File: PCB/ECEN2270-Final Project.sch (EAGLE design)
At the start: 39 parts, among them J1 USB_MINI-B_SMT, J2 POWER_JACK, Q1 310mA/60V/1.6Ω, Q2 2.5A/30V/105mΩ, U1 FT231XS, U2 LMV358, U3 ATMEGA328P_TQFP, U4 3.3V/150mA, Y2 16MHz

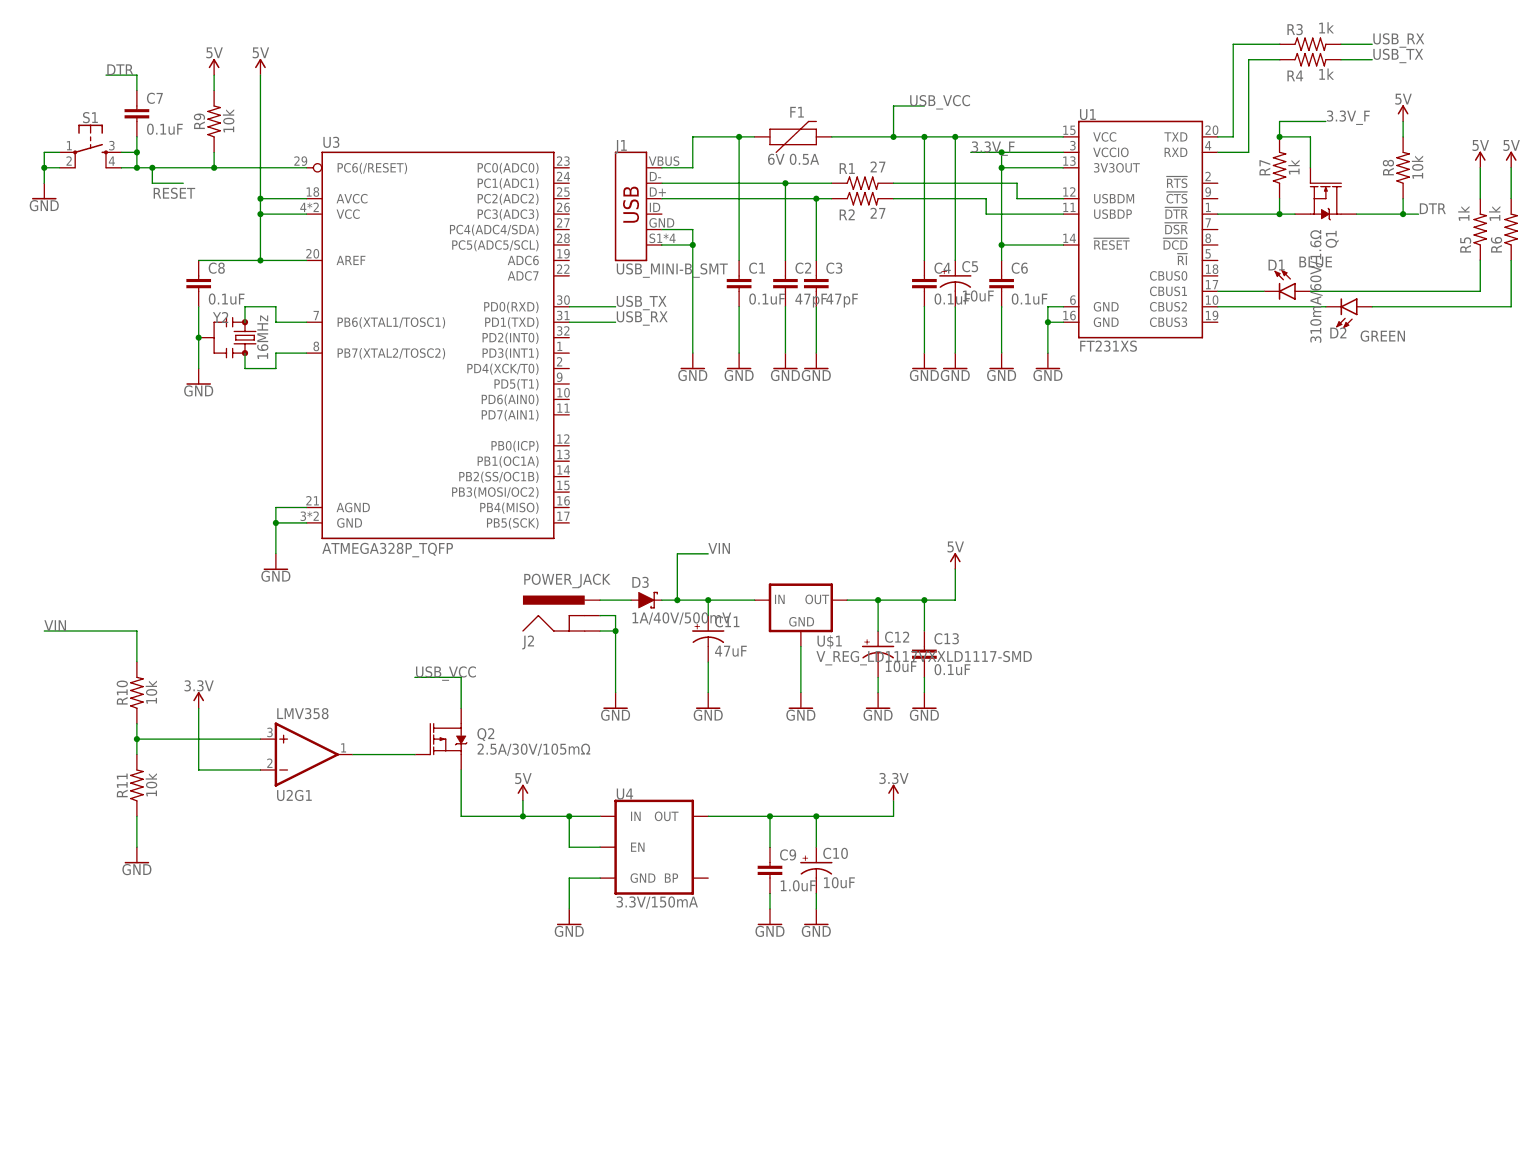
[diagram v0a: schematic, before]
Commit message: Added ICSP Header For Arduino
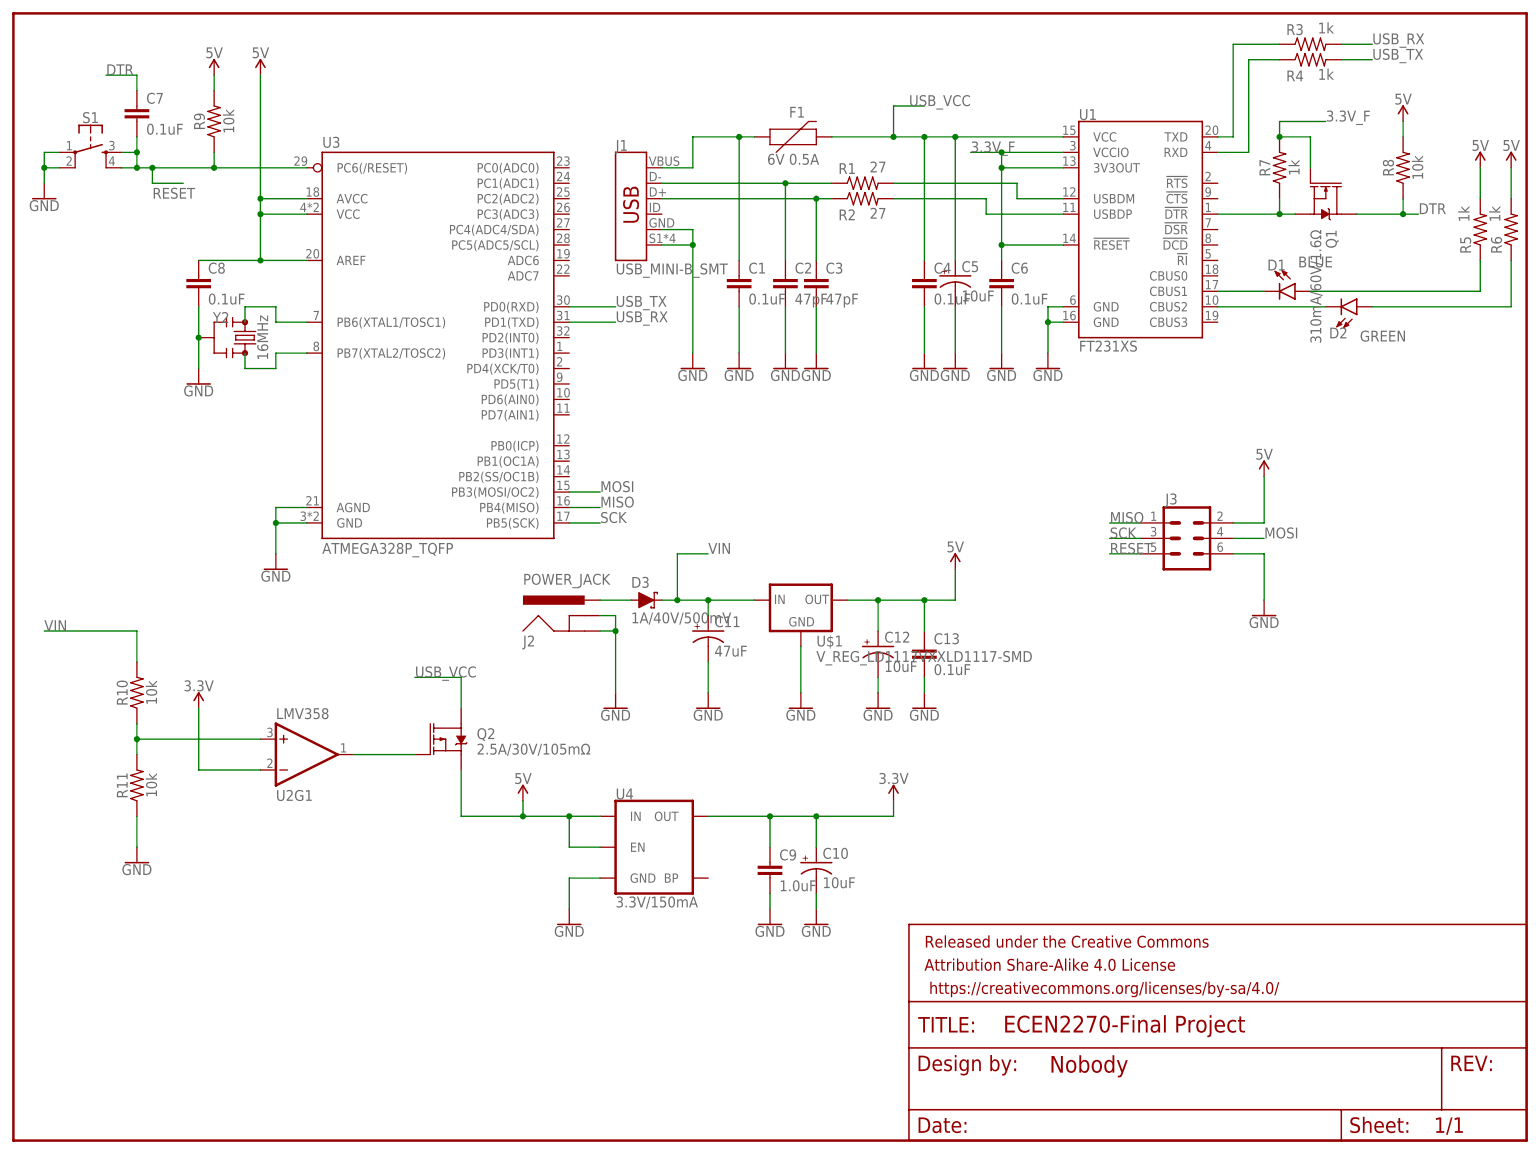
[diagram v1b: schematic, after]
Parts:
- added FRAME1: FRAME-LETTERNO_PACKAGE, SparkFun-Aesthetics:FRAME-LETTERNO_PACKAGE
- added J3: (no value), SparkFun-Connectors:CONN_03X22X3_SILK_MALE_PTH
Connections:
- new net MISO: J3.1, U3.PB4(MISO)
- new net MOSI: J3.4, U3.PB3(MOSI/OC2)
- new net SCK: J3.3, U3.PB5(SCK)
- net 5V: now also J3.2
- net GND: now also J3.6
- net RESET: now also J3.5
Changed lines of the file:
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@@
 <part name="C13" library="SparkFun-Capacitors" deviceset="0.1UF" device="-0603-25V-(+80/-20%)" value="0.1uF"/>
 <part name="SUPPLY9" library="SparkFun-PowerSymbols" deviceset="5V" device=""/>
+<part name="FRAME1" library="SparkFun-Aesthetics" deviceset="FRAME-LETTER" device="NO_PACKAGE"/>
+<part name="J3" library="SparkFun-Connectors" deviceset="CONN_03X2" device="2X3_SILK_MALE_PTH"/>
+<part name="SUPPLY10" library="SparkFun-PowerSymbols" deviceset="5V" device=""/>
+<part name="GND21" library="SparkFun-PowerSymbols" deviceset="GND" device=""/>
 </parts>
 <sheets>
@@
 <instance part="SUPPLY9" gate="G$1" x="154.94" y="93.98" smashed="yes">
 <attribute name="VALUE" x="154.94" y="96.774" size="1.778" layer="96" align="bottom-center"/>
+</instance>
+<instance part="FRAME1" gate="G$1" x="0" y="0" smashed="yes"/>
+<instance part="FRAME1" gate="V" x="147.32" y="0" smashed="yes">
+<attribute name="LAST_DATE_TIME" x="160.02" y="1.27" size="2.54" layer="94" font="vector"/>
+<attribute name="SHEET" x="233.68" y="1.27" size="2.54" layer="94" font="vector"/>
+<attribute name="DRAWING_NAME" x="162.814" y="17.78" size="2.7432" layer="94" font="vector"/>
+<attribute name="DESIGNER" x="170.434" y="11.176" size="2.7432" layer="94" font="vector"/>
+</instance>
+<instance part="J3" gate="G$1" x="193.04" y="99.06" smashed="yes">
+<attribute name="NAME" x="189.484" y="104.648" size="1.778" layer="95" font="vector"/>
+<attribute name="VALUE" x="189.738" y="93.218" size="1.778" layer="96" font="vector" align="top-left"/>
+</instance>
+<instance part="SUPPLY10" gate="G$1" x="205.74" y="109.22" smashed="yes">
+<attribute name="VALUE" x="205.74" y="112.014" size="1.778" layer="96" align="bottom-center"/>
+</instance>
+<instance part="GND21" gate="1" x="205.74" y="86.36" smashed="yes">
+<attribute name="VALUE" x="205.74" y="86.106" size="1.778" layer="96" align="top-center"/>
 </instance>
 </instances>
@@
 <wire x1="149.86" y1="73.66" x2="149.86" y2="76.2" width="0.1524" layer="91"/>
 </segment>
+<segment>
+<pinref part="J3" gate="G$1" pin="6"/>
+<wire x1="200.66" y1="96.52" x2="205.74" y2="96.52" width="0.1524" layer="91"/>
+<wire x1="205.74" y1="96.52" x2="205.74" y2="88.9" width="0.1524" layer="91"/>
+<pinref part="GND21" gate="1" pin="GND"/>
+</segment>
 </net>
 <net name="3.3V_F" class="0">
@@
 <wire x1="154.94" y1="88.9" x2="154.94" y2="93.98" width="0.1524" layer="91"/>
 <pinref part="SUPPLY9" gate="G$1" pin="5V"/>
+</segment>
+<segment>
+<pinref part="J3" gate="G$1" pin="2"/>
+<wire x1="200.66" y1="101.6" x2="205.74" y2="101.6" width="0.1524" layer="91"/>
+<wire x1="205.74" y1="101.6" x2="205.74" y2="109.22" width="0.1524" layer="91"/>
+<pinref part="SUPPLY10" gate="G$1" pin="5V"/>
 </segment>
 </net>
@@
 <label x="22.86" y="154.94" size="1.778" layer="95"/>
 </segment>
+<segment>
+<pinref part="J3" gate="G$1" pin="5"/>
+<wire x1="185.42" y1="96.52" x2="180.34" y2="96.52" width="0.1524" layer="91"/>
+<label x="180.34" y="96.52" size="1.778" layer="95"/>
+</segment>
 </net>
 <net name="N$13" class="0">
@@
 </segment>
 </net>
+<net name="MISO" class="0">
+<segment>
+<pinref part="J3" gate="G$1" pin="1"/>
+<wire x1="185.42" y1="101.6" x2="180.34" y2="101.6" width="0.1524" layer="91"/>
+<label x="180.34" y="101.6" size="1.778" layer="95"/>
+</segment>
+<segment>
+<pinref part="U3" gate="U1" pin="PB4(MISO)"/>
+<wire x1="91.44" y1="104.14" x2="96.52" y2="104.14" width="0.1524" layer="91"/>
+<label x="96.52" y="104.14" size="1.778" layer="95"/>
+</segment>
+</net>
+<net name="SCK" class="0">
+<segment>
+<pinref part="J3" gate="G$1" pin="3"/>
+<wire x1="185.42" y1="99.06" x2="180.34" y2="99.06" width="0.1524" layer="91"/>
+<label x="180.34" y="99.06" size="1.778" layer="95"/>
+</segment>
+<segment>
+<pinref part="U3" gate="U1" pin="PB5(SCK)"/>
+<wire x1="91.44" y1="101.6" x2="96.52" y2="101.6" width="0.1524" layer="91"/>
+<label x="96.52" y="101.6" size="1.778" layer="95"/>
+</segment>
+</net>
+<net name="MOSI" class="0">
+<segment>
+<pinref part="J3" gate="G$1" pin="4"/>
+<wire x1="200.66" y1="99.06" x2="205.74" y2="99.06" width="0.1524" layer="91"/>
+<label x="205.74" y="99.06" size="1.778" layer="95"/>
+</segment>
+<segment>
+<pinref part="U3" gate="U1" pin="PB3(MOSI/OC2)"/>
+<wire x1="91.44" y1="106.68" x2="96.52" y2="106.68" width="0.1524" layer="91"/>
+<label x="96.52" y="106.68" size="1.778" layer="95"/>
+</segment>
+</net>

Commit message: Replaced Mini USB with Micro
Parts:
- J1: value USB_MINI-B_SMT -> (none); device SparkFun-Connectors:USB_MINI-B_SMT -> SparkFun-Connectors:USB_MICRO-B_FEMALE-SMT
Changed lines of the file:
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@@
 <parts>
 <part name="U1" library="SparkFun-IC-Comms" deviceset="FT231X" device="S" value="FT231XS"/>
-<part name="J1" library="SparkFun-Connectors" deviceset="USB_MINI-B" device="_SMT"/>
+<part name="J1" library="SparkFun-Connectors" deviceset="USB_MICRO-B" device="_FEMALE-SMT"/>
 <part name="F1" library="SparkFun-Fuses" deviceset="PPTC" device="_6V500MA" value="6V 0.5A"/>
 <part name="GND1" library="SparkFun-PowerSymbols" deviceset="GND" device=""/>
@@
 <attribute name="VALUE" x="175.26" y="131.572" size="1.778" layer="96" align="top-left"/>
 </instance>
-<instance part="J1" gate="G$1" x="101.6" y="152.4" smashed="yes">
+<instance part="J1" gate="J1" x="101.6" y="152.4" smashed="yes">
 <attribute name="VALUE" x="99.06" y="142.494" size="1.778" layer="96" font="vector" rot="MR180" align="top-left"/>
 <attribute name="NAME" x="99.06" y="162.814" size="1.778" layer="95" font="vector"/>
@@
 <net name="GND" class="0">
 <segment>
-<pinref part="J1" gate="G$1" pin="SHIELD"/>
+<pinref part="J1" gate="J1" pin="SHIELD"/>
 <wire x1="106.68" y1="147.32" x2="111.76" y2="147.32" width="0.1524" layer="91"/>
 <pinref part="GND1" gate="1" pin="GND"/>
 <wire x1="111.76" y1="147.32" x2="111.76" y2="129.54" width="0.1524" layer="91"/>
-<pinref part="J1" gate="G$1" pin="GND"/>
+<pinref part="J1" gate="J1" pin="GND"/>
 <wire x1="106.68" y1="149.86" x2="111.76" y2="149.86" width="0.1524" layer="91"/>
 <wire x1="111.76" y1="149.86" x2="111.76" y2="147.32" width="0.1524" layer="91"/>
@@
 <net name="N$1" class="0">
 <segment>
-<pinref part="J1" gate="G$1" pin="VBUS"/>
+<pinref part="J1" gate="J1" pin="VBUS"/>
 <wire x1="106.68" y1="160.02" x2="111.76" y2="160.02" width="0.1524" layer="91"/>
 <wire x1="111.76" y1="160.02" x2="111.76" y2="165.1" width="0.1524" layer="91"/>
@@
 <net name="N$2" class="0">
 <segment>
-<pinref part="J1" gate="G$1" pin="D-"/>
+<pinref part="J1" gate="J1" pin="D-"/>
 <pinref part="R1" gate="G$1" pin="1"/>
 <wire x1="106.68" y1="157.48" x2="127" y2="157.48" width="0.1524" layer="91"/>
@@
 <net name="N$4" class="0">
 <segment>
-<pinref part="J1" gate="G$1" pin="D+"/>
+<pinref part="J1" gate="J1" pin="D+"/>
 <pinref part="R2" gate="G$1" pin="1"/>
 <wire x1="106.68" y1="154.94" x2="132.08" y2="154.94" width="0.1524" layer="91"/>
